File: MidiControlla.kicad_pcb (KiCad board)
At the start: 2 copper layers, 4 parts, among them U1 TCRT5000, U2 TCRT5000, U3 TCRT5000, U4 TCRT5000

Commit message: Add espressif c3
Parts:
- added U5: ESP32-S3-DevKitC, Espressif:ESP32-S3-DevKitC, B.Cu at (128.2, 85.1)

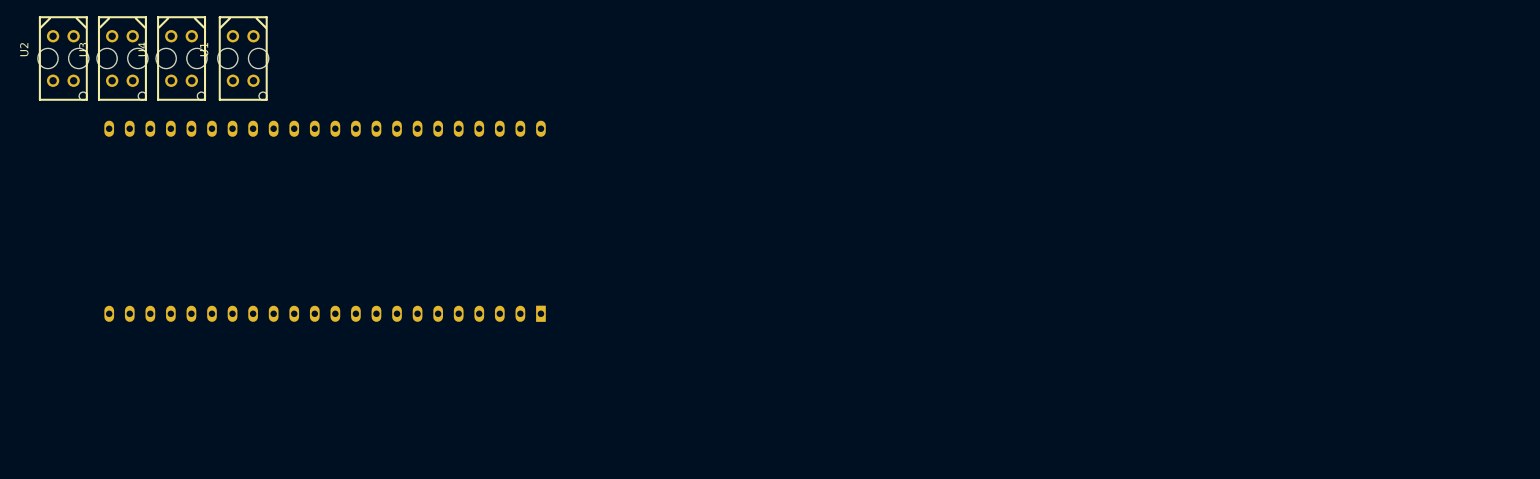
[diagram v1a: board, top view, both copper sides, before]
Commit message: Add footprints
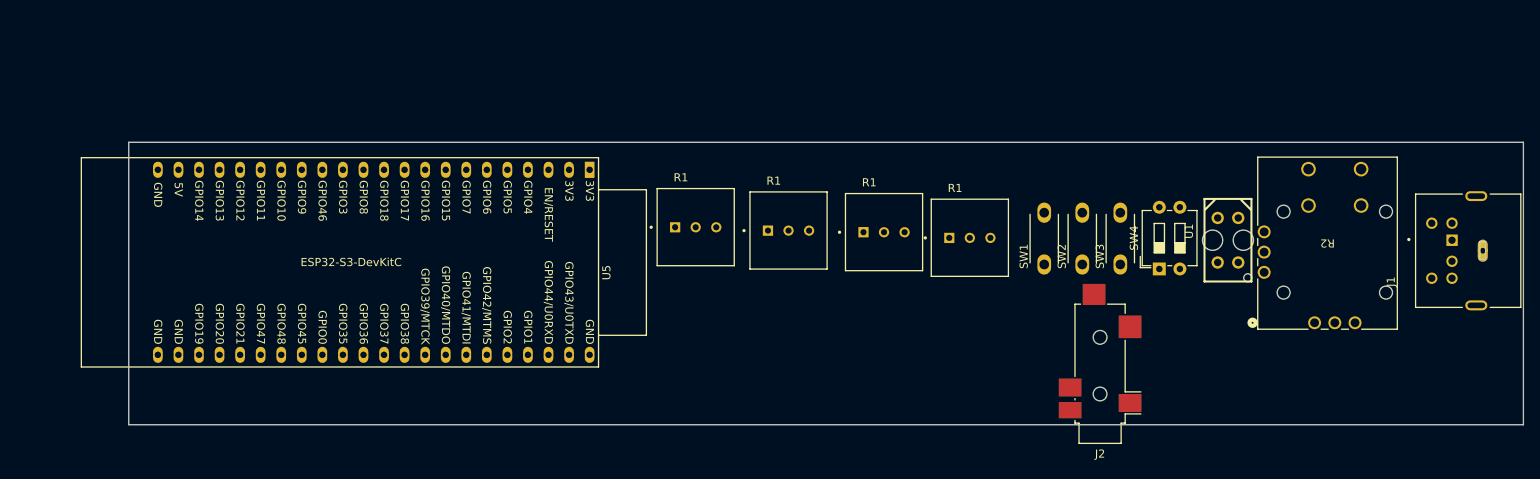
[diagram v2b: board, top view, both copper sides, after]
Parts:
- removed U2, U3, U4: TCRT5000, jlc_footprints:OPTO-TH_TCRT5000
- added J1: Midi OUT, MD-60SM:MD-60SM, F.Cu at (244.6, 77.3)
- added J2: Midi Out TRS, Connector_Audio:Jack_3.5mm_CUI_SJ2-3593D-SMT_Horizontal, F.Cu at (197.3, 92.5)
- added R1: COM-09806, COM-09806:COM-09806, F.Cu at (158.8, 74.8)
- added R1: COM-09806, COM-09806:COM-09806, F.Cu at (181.2, 75.7)
- added R1: COM-09806, COM-09806:COM-09806, F.Cu at (147.3, 74.4)
- added R1: COM-09806, COM-09806:COM-09806, F.Cu at (170.6, 75.0)
- added R2: THB001P, THB001P:THB001P, F.Cu at (223.8, 86.2)
- added SW1: SW_Push, pts636:pts636, F.Cu at (190.4, 79.0)
- added SW2: SW_Push, pts636:pts636, F.Cu at (195.1, 79.0)
- added SW3: SW_Push, pts636:pts636, F.Cu at (199.8, 79.0)
- added SW4: SW_DIP_x02, Button_Switch_THT:SW_DIP_SPSTx02_Slide_6.7x6.64mm_W7.62mm_P2.54mm_LowProfile, F.Cu at (204.6, 79.5)
- U5: moved to F.Cu
- moved U1 123.7 mm to (213.1, 76.0)
- moved U5 18.8 mm to (134.2, 67.3), turned to -90 degrees
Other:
- board outline added: 172.3 x 34.9 mm
